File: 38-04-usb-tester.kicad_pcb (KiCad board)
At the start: 2 copper layers, 125.9 x 97.8 mm, 67 parts, among them J1 Conn_1x05, J2 USB_C_12401832E402A, J3 USB_C_12401832E402A, J4 USB_Micro-B_KH-MICRO5P-JN, J5 USB_Mini-B_U-M-M5DD-W-1, J6 USB3_A_HC-USB3.0-L168-WP, SW1 SW_SPDT, SW2 ZX-1.27BM-4PSMD, U1 STM32C031K6Tx

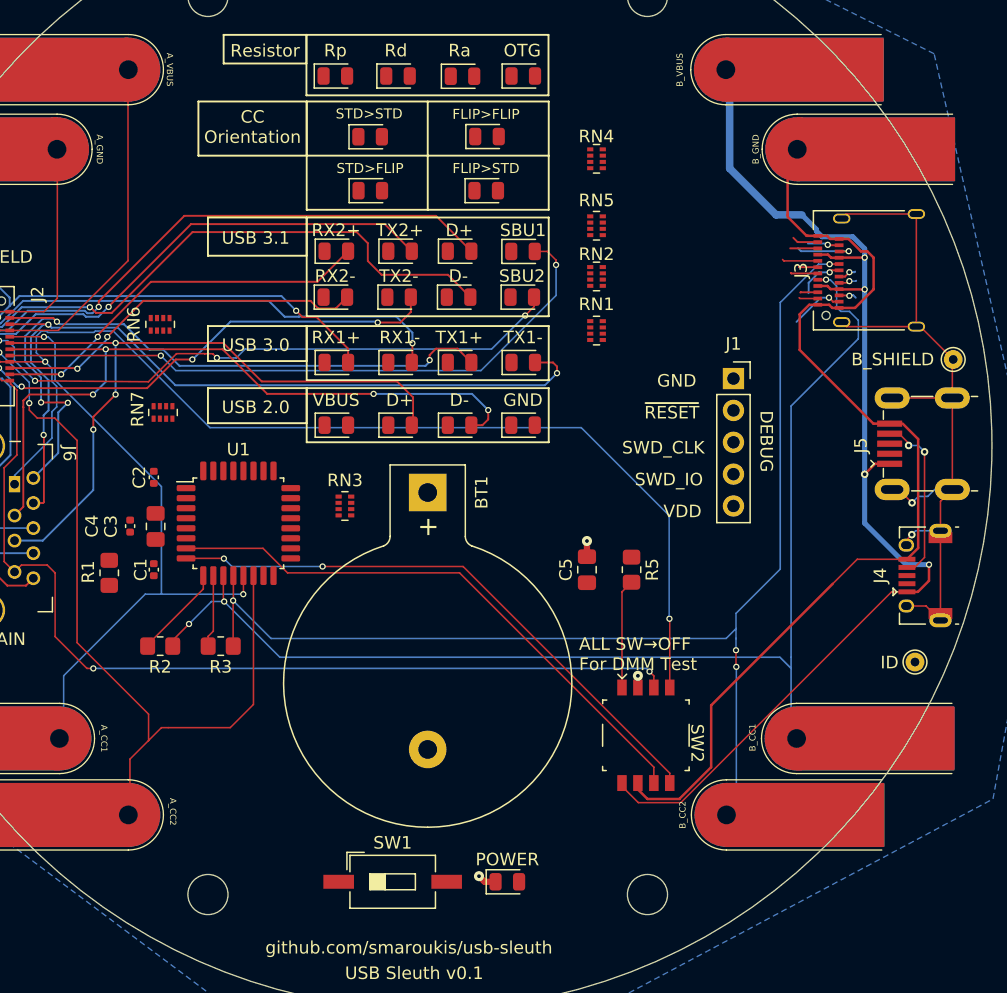
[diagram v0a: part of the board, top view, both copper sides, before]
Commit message: routing LEDs, started USB B side
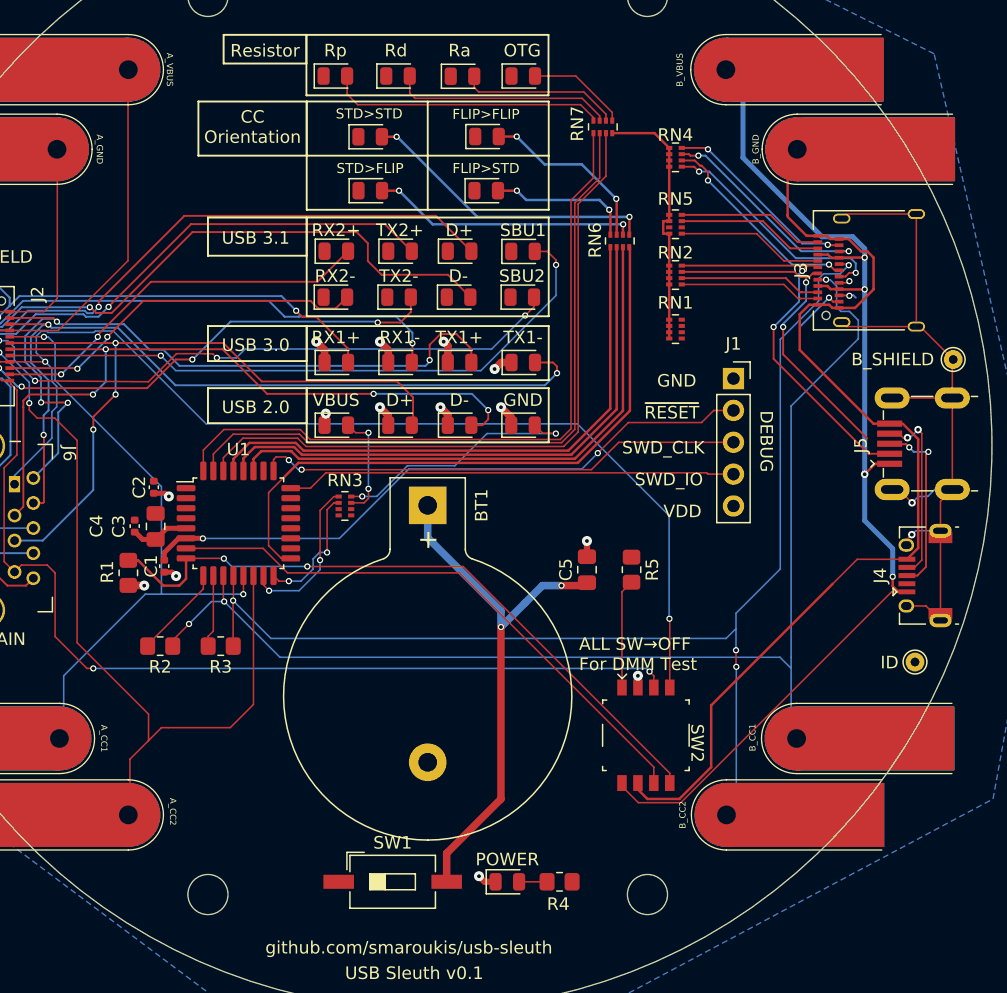
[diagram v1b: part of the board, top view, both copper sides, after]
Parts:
- added R4: 1K, Resistor_SMD:R_0805_2012Metric_Pad1.20x1.40mm_HandSolder, F.Cu at (165.5, 145.3)
- moved RN7 41.8 mm to (168.9, 85.1)
- moved RN6 37.3 mm to (170.3, 94.2), turned to -90 degrees
- moved RN1 6.30 mm to (174.7, 101.2)
- moved RN2 6.30 mm to (174.7, 96.9)
- moved RN4 6.30 mm to (174.7, 87.5)
- moved RN5 6.30 mm to (174.7, 92.8)
- moved R1 1.52 mm to (131.1, 120.7)
- moved BT1 1.02 mm to (154.9, 115.3)
- moved C1 0.88 mm to (133.9, 120.1)
- moved C2 0.79 mm to (133.1, 113.8)
- moved C4 0.37 mm to (131.6, 116.9)
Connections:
- net /B_SSRTx1+ renamed /B_SSTx1+
- D1 pad 2: /PWR_LED -> Net-(D1-A)
- J3 pad A3: /B_SSRx1- -> /B_SSTx1-
- RN1 pad 7: /PWR_LED -> unconnected-(RN1-R2.2-Pad7)
- RN2 pad 2: /B_SSRx1- -> /B_SSTx1-
- RN6 pad 1: Net-(D17-A) -> Net-(D12-A)
- RN6 pad 2: Net-(D16-A) -> Net-(D15-A)
- RN6 pad 3: Net-(D15-A) -> Net-(D16-A)
- RN6 pad 4: Net-(D12-A) -> Net-(D17-A)
- RN6 pad 5: /CC_aa -> /CC_ba
- RN6 pad 6: /CC_ab -> /CC_bb
- RN6 pad 7: /CC_bb -> /CC_ab
- RN6 pad 8: /CC_ba -> /CC_aa
- U1 pad 30: /CC_Rp_LED -> /E_MARKER_LED
- U1 pad 32: /E_MARKER_LED -> /CC_Rp_LED
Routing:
- net /CC_Rp_LED: track 0.00 -> 56.7 mm
- net /CC_Rd_LED: track 0.00 -> 56.0 mm
- net /E_MARKER_LED: track 0.00 -> 55.5 mm
- net /CC_aa: track 0.00 -> 51.0 mm
- net /~{RESET}: track 0.00 -> 50.7 mm, vias 0 -> 2
- net /CC_ba: track 0.00 -> 46.1 mm
- net /CC_bb: track 0.00 -> 45.8 mm
- net /CC_ab: track 0.00 -> 45.6 mm
- net Net-(BT1-+): track 0.00 -> 42.6 mm, vias 0 -> 2
- net /B_D1+: track 2.17 -> 42.0 mm, vias 0 -> 4
- net /SWCLK_BOOT0: track 0.00 -> 39.0 mm, vias 0 -> 2
- net /SWDIO: track 0.00 -> 35.9 mm
- net /B_D1-: track 1.50 -> 31.8 mm, vias 0 -> 2
- net Net-(D12-A): track 0.00 -> 23.8 mm, vias 0 -> 2
- net Net-(D21-A): track 0.00 -> 22.1 mm
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
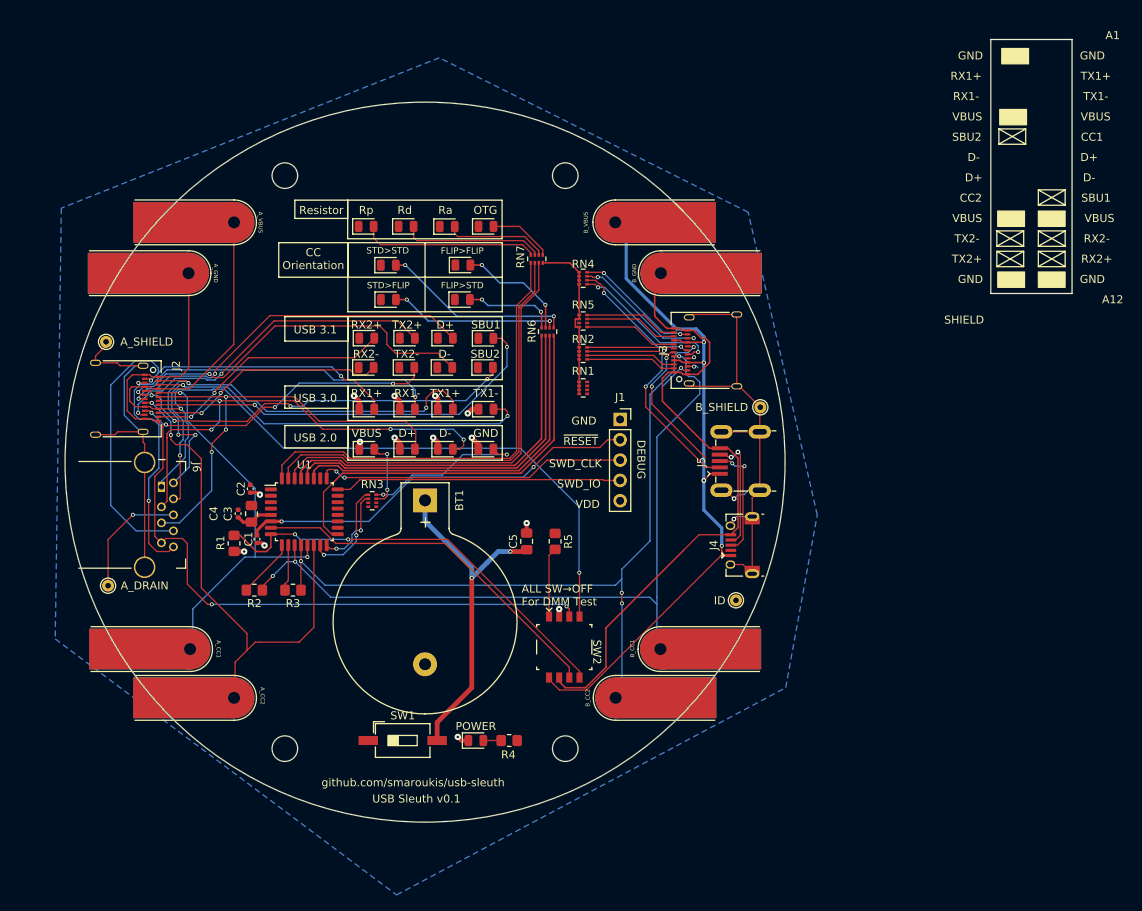
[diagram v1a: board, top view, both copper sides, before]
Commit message: via size change refactoring DRC errors
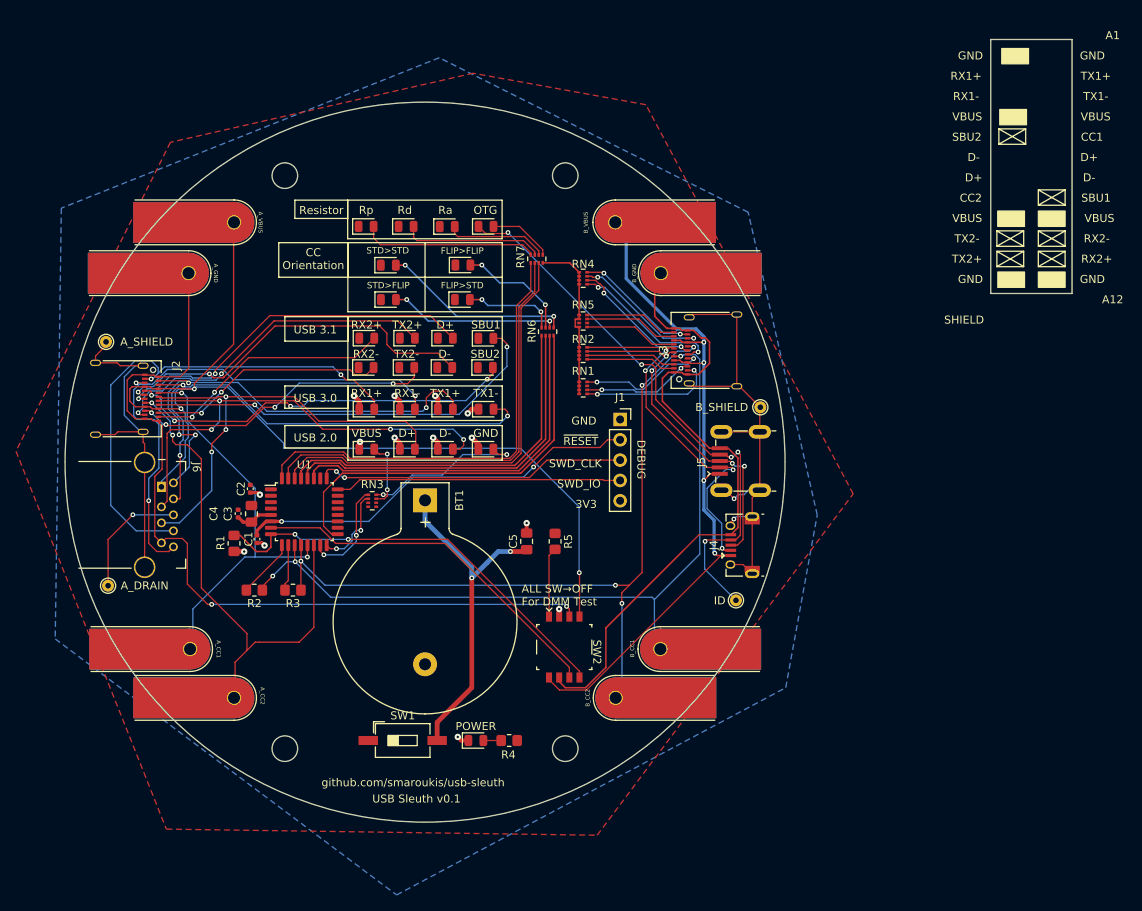
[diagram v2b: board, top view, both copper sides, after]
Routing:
- net /ID: track 14.6 -> 71.3 mm, vias 2 -> 5
- net /B_D1-: track 31.8 -> 47.7 mm, vias 2 -> 4
- net /B_SBU2: track 0.88 -> 16.1 mm, vias 1 -> 2
- net /B_SSRx1+: track 4.13 -> 17.0 mm, vias 1 -> 2
- net /B_SSRx1-: track 1.42 -> 14.0 mm, vias 1 -> 2
- net /B_D1+: track 42.0 -> 44.1 mm
- net /A_VBUS: track 123.1 -> 124.5 mm, vias 2 -> 3
- net /B_CC2_SENS: track 95.8 -> 96.6 mm, vias 4 -> 5
- net /B_VBUS_A4: track 89.5 -> 90.1 mm
- net /A_SSRx1-: track 67.6 -> 68.1 mm
- added copper zone on F.Cu, net VCC
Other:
- board text added: "3V3"
- board text removed: "VDD"

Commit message: more layout DRC fixes
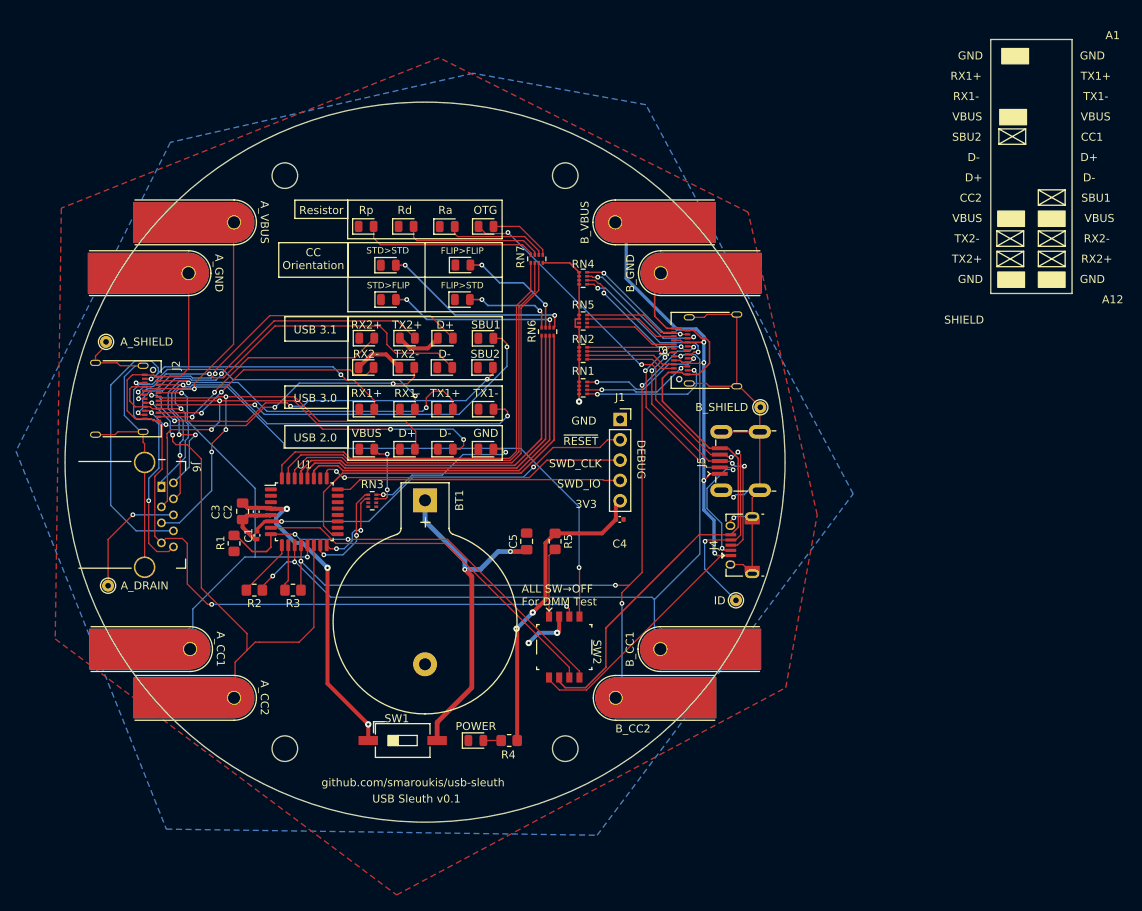
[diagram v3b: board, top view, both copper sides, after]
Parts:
- moved C4 47.7 mm to (179.3, 117.7), turned to 180 degrees
- moved C2 2.96 mm to (133.8, 116.7)
- moved C3 1.15 mm to (132.1, 116.6)
- moved C1 0.48 mm to (133.9, 119.6)
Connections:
- U1 pad 4: VDD -> VCC
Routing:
- net VCC: track 21.2 -> 101.8 mm, vias 0 -> 6
- net GND: track 25.7 -> 26.0 mm, vias 14 -> 2
- added copper zone on F.Cu, net GND
- added copper zone on B.Cu, net VCC
- removed copper zone on B.Cu, net GND
- removed copper zone on F.Cu, net VCC

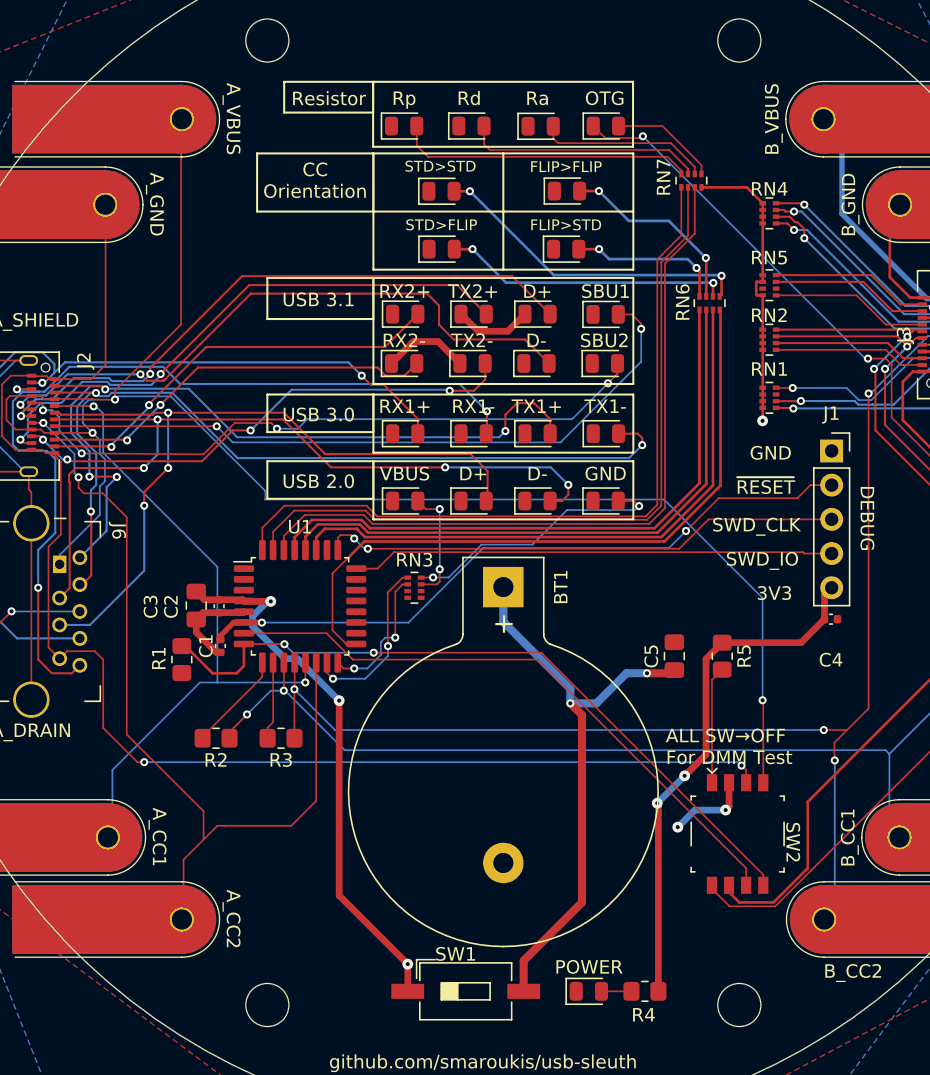
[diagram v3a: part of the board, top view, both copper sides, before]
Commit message: more layouts and DRC routing
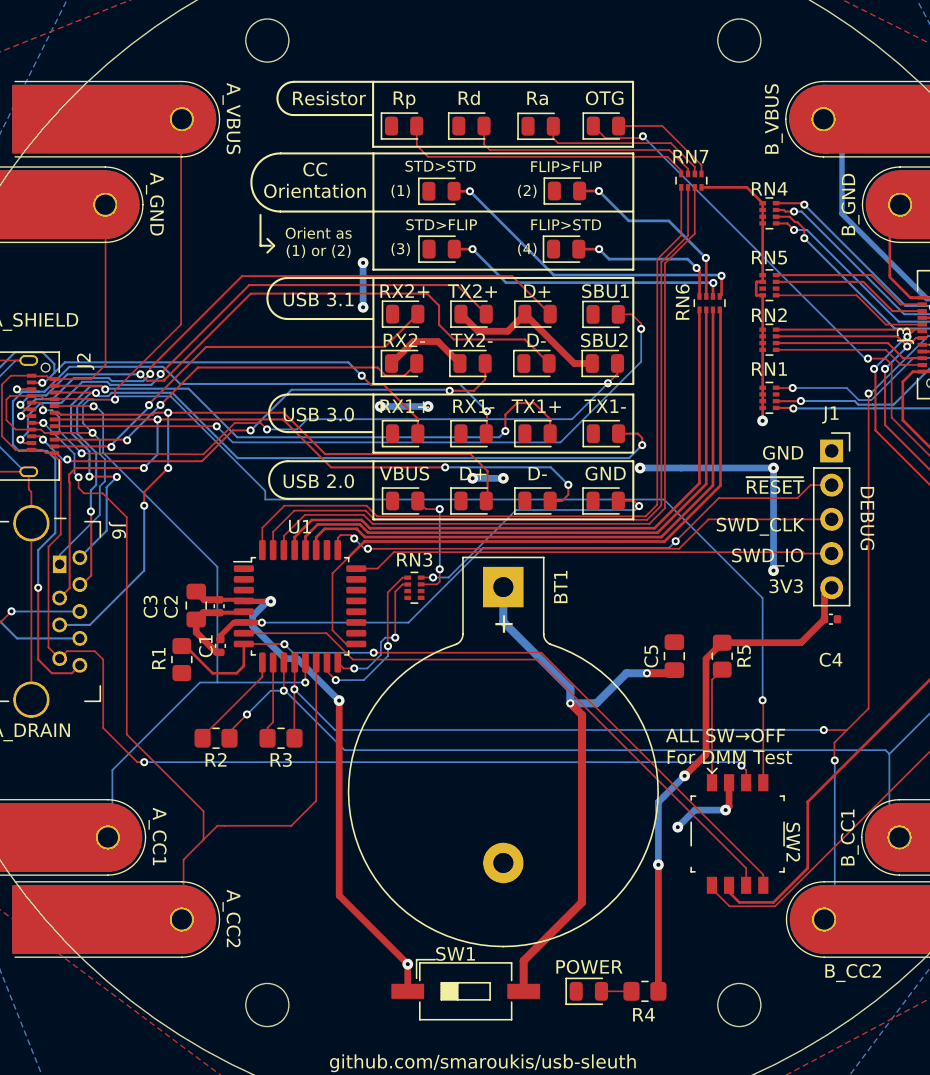
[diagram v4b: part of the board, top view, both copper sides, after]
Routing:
- net GND: track 26.0 -> 59.1 mm, vias 2 -> 11
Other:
- board text added: "(1)"
- board text added: "(2)"
- board text added: "(3)"
- board text added: "(4)"
- board text added: "Orient as (1) or (2)"

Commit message: board layouts and edge cut edits
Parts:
- moved R4 5.16 mm to (166.4, 140.2), turned to -90 degrees
- moved SW1 3.07 mm to (154.9, 146.6)
- moved H8 2.54 mm to (194.3, 103.6)
- moved D1 2.40 mm to (163.3, 146.6)
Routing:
- net GND: track 59.1 -> 63.3 mm
- net Net-(D1-A): track 2.23 -> 6.22 mm
- net VCC: track 101.7 -> 98.1 mm
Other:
- outline, holes or cut-outs redrawn
- board text added: "(A>B)"
- board text added: "TODO - LOGO"
